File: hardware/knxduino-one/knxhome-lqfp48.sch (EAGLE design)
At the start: 47 parts, among them IC1 LDL1117S33, IC2 STM32G071CBT6, IC3 BD9G101, P1 B10B-PH-K, P2 B10B-PH-K, P3 B6B-PH-K, U1 OSCILLATOR5X3-PIN1-INDICATED

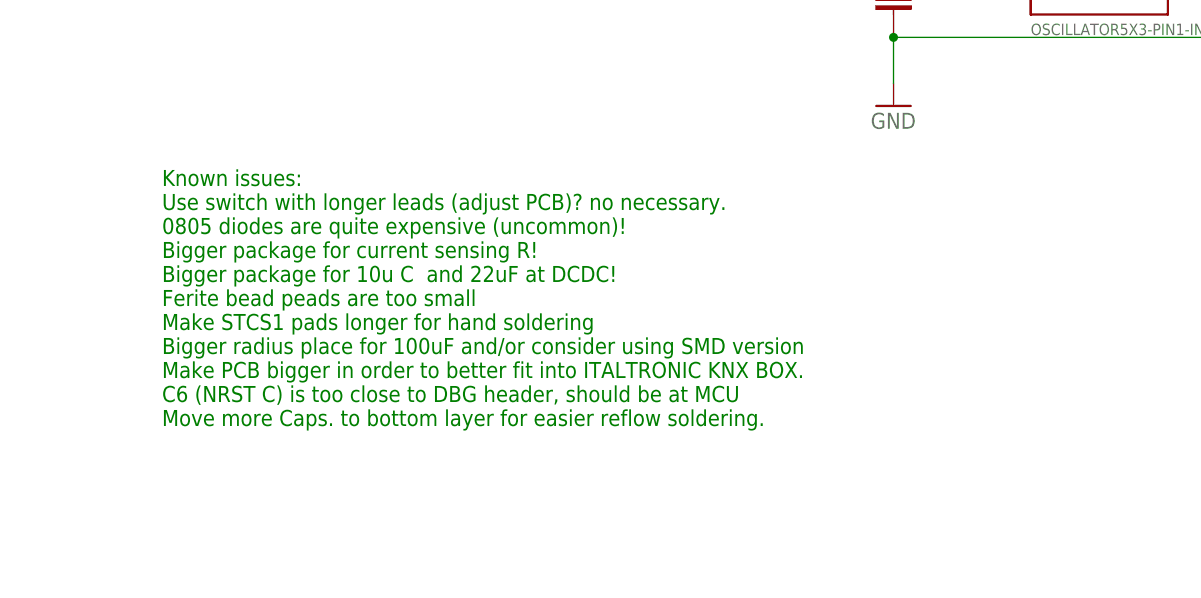
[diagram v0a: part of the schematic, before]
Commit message: STM32G071 LQFP48 version
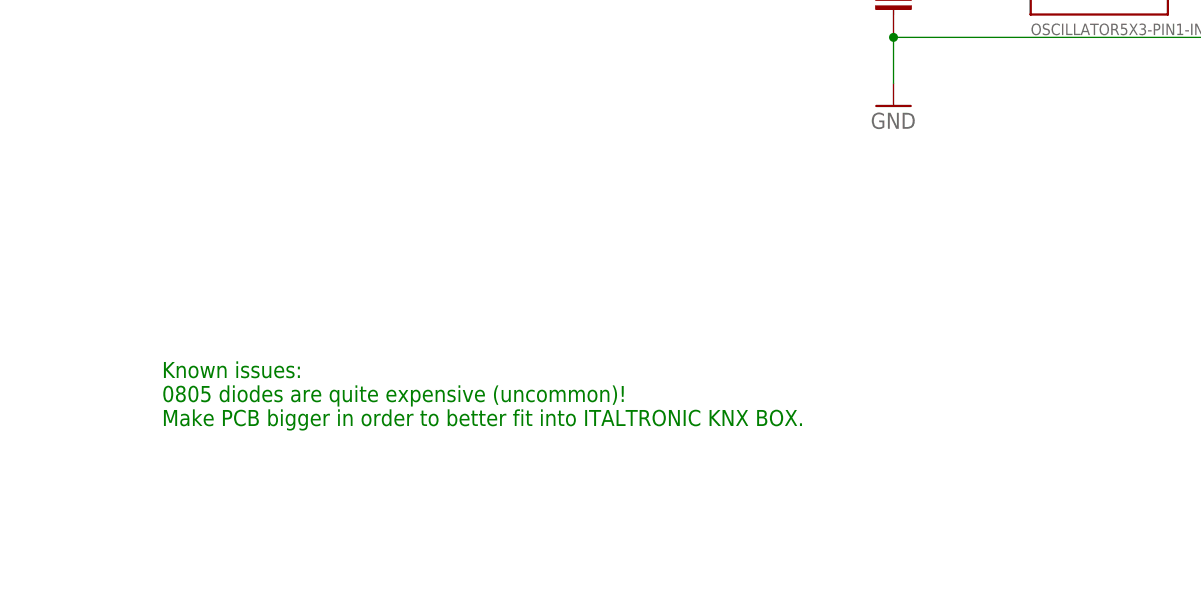
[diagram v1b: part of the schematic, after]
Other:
- note added: "Known issues: 0805 diodes are quite expensive (uncommon)! Make PCB bigger in order to better fit into ITALTRONIC KNX BOX."
- note removed: "Known issues: Use switch with longer leads (adjust PCB)? no necessary. 0805 diodes are quite expensive (uncommon)! Bigger package for current sensing R! Bigger package for 10u C and 22uF at DCDC! Ferite bead peads are too small Make STCS1 pads longer for hand soldering Bigger radius place for 100uF and/or consider using SMD version Make PCB bigger in order to better fit into ITALTRONIC KNX BOX. C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"
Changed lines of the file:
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@@
  hysteresis to COMP's selectable hysteresis</text>
 <text x="-162.56" y="2.54" size="1.778" layer="91">Known issues:
-Use switch with longer leads (adjust PCB)? no necessary.
 0805 diodes are quite expensive (uncommon)!
-Bigger package for current sensing R!
-Bigger package for 10u C  and 22uF at DCDC!
-Ferite bead peads are too small
-Make STCS1 pads longer for hand soldering
-Bigger radius place for 100uF and/or consider using SMD version
 Make PCB bigger in order to better fit into ITALTRONIC KNX BOX.
-C6 (NRST C) is too close to DBG header, should be at MCU
-Move more Caps. to bottom layer for easier reflow soldering.</text>
+</text>
 </plain>
 <instances>
